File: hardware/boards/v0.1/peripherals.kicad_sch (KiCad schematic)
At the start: 8 parts, among them IC2 DA7280-00FVC, J6 VLV101040A, U21 LSM6DS3

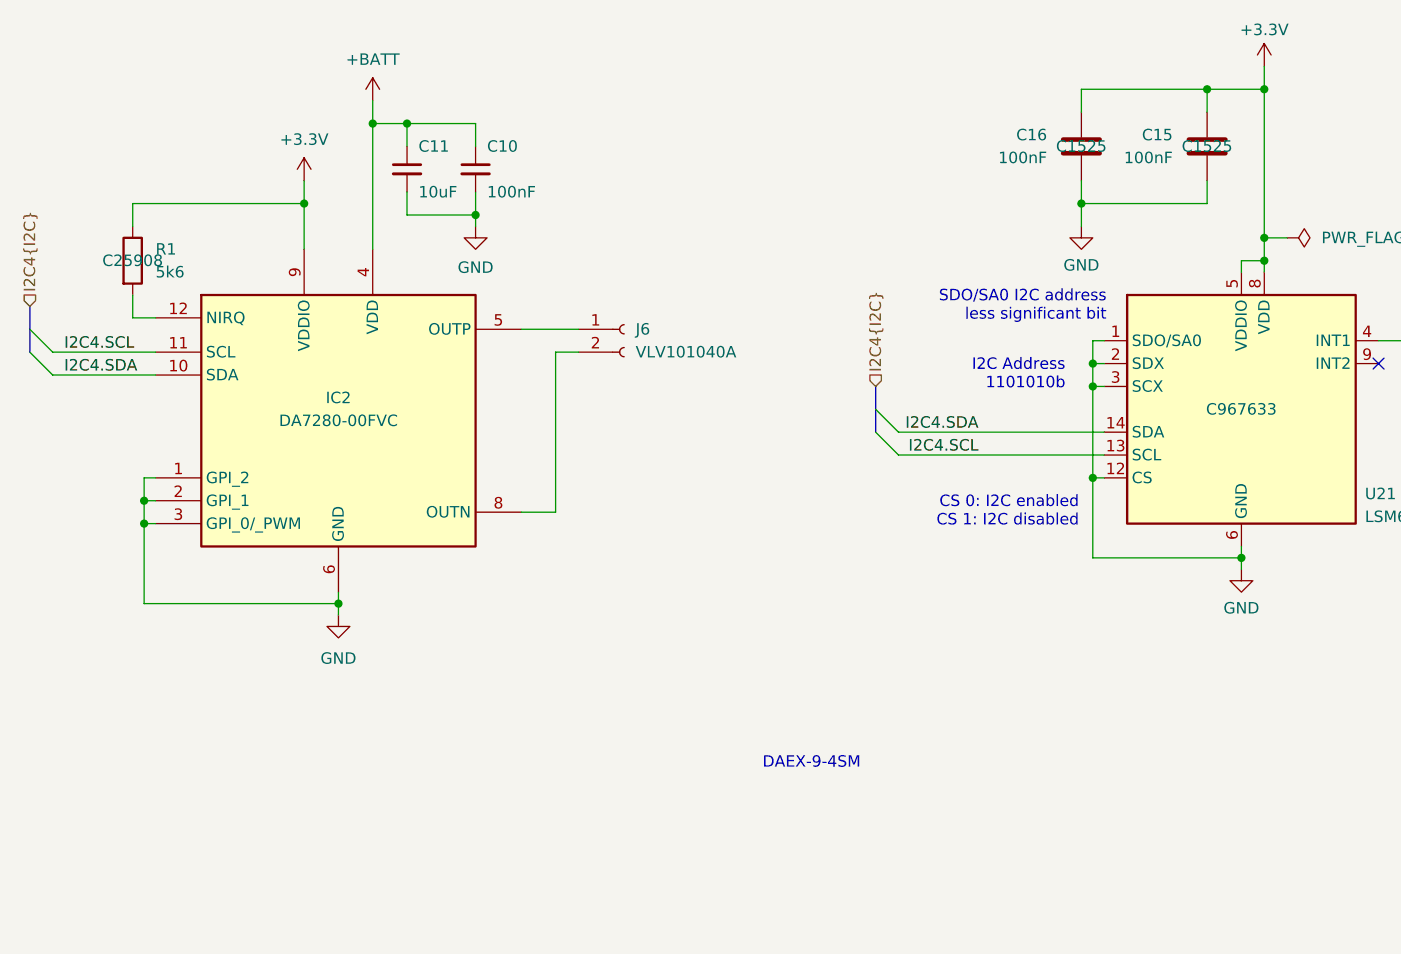
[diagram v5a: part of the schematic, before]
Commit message: feat: swap out of stock components
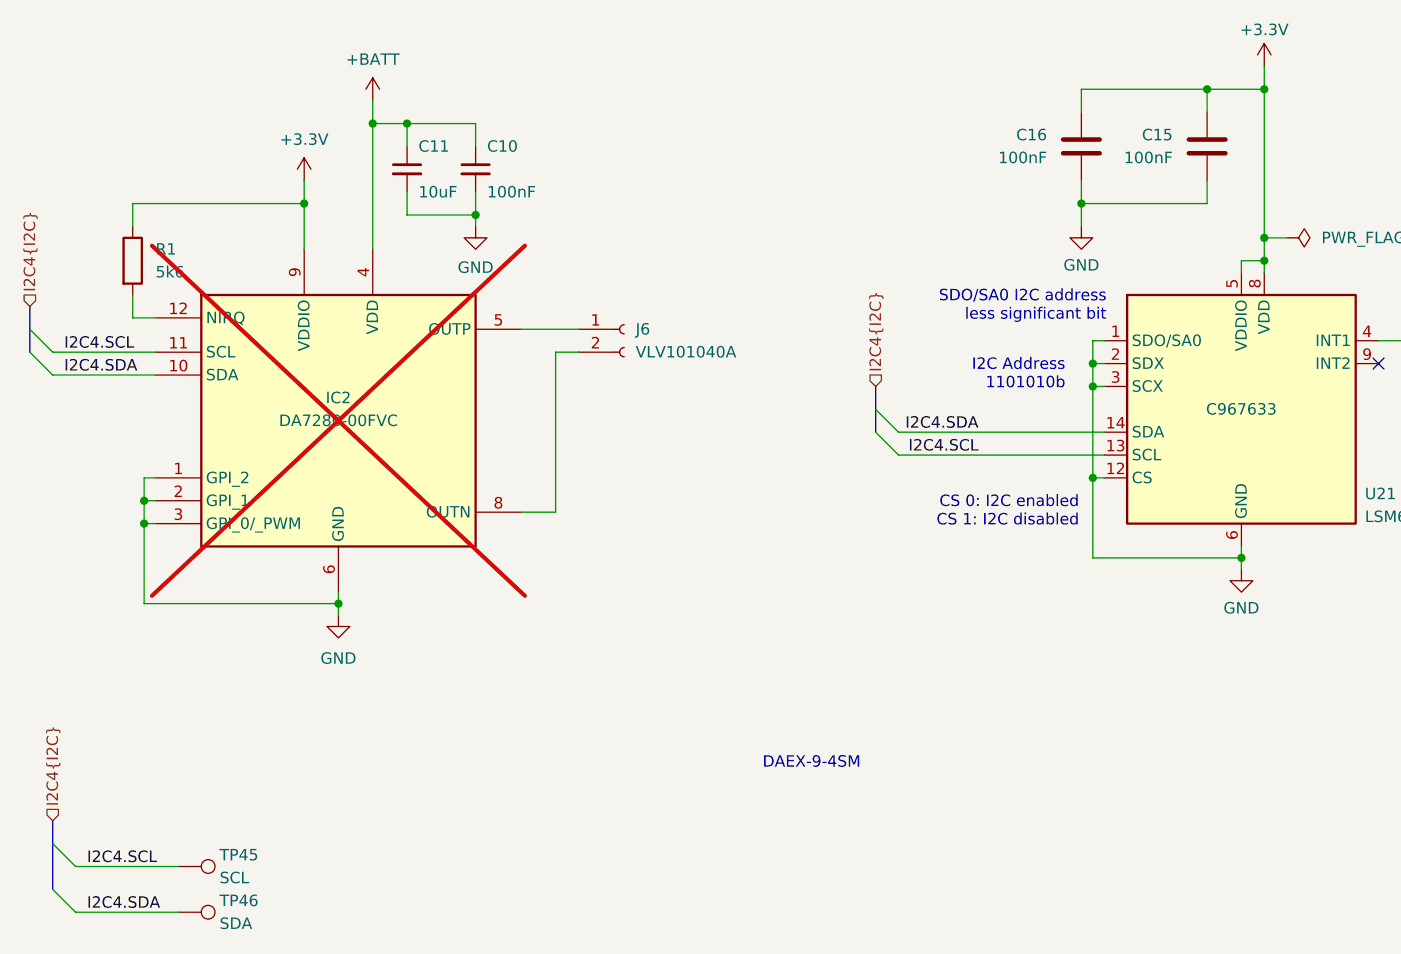
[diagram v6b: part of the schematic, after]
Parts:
- added TP45: SCL, TestPoint:TestPoint_Pad_D1.0mm, symbol Connector:TestPoint
- added TP46: SDA, TestPoint:TestPoint_Pad_D1.0mm, symbol Connector:TestPoint
- IC2: Manufacturer_Name Renesas Electronics -> (none); Manufacturer_Part_Number DA7280-00FVC -> (none); now not fitted
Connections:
- net I2C4.SCL: now also TP45.1
- net I2C4.SDA: now also TP46.1
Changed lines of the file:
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@@
+	)
+	(bus_entry
+		(at 33.02 110.49)
+		(size -2.54 -2.54)
+		(stroke
+			(width 0)
+			(type default)
+		)
 	)
 	(bus_entry
@@
 	)
 	(bus_entry
+		(at 33.02 115.57)
+		(size -2.54 -2.54)
+		(stroke
+			(width 0)
+			(type default)
+		)
+	)
+	(bus_entry
 		(at 30.48 53.34)
 		(size -2.54 -2.54)
@@
 		)
 	)
+	(wire
+		(pts
+			(xy 33.02 115.57) (xy 44.45 115.57)
+		)
+		(stroke
+			(width 0)
+			(type default)
+		)
+	)
 	(bus
 		(pts
@@
 	(wire
 		(pts
+			(xy 33.02 110.49) (xy 44.45 110.49)
+		)
+		(stroke
+			(width 0)
+			(type default)
+		)
+	)
+	(wire
+		(pts
 			(xy 39.37 46.99) (xy 39.37 49.53)
 		)
@@
 		)
 	)
+	(bus
+		(pts
+			(xy 30.48 107.95) (xy 30.48 113.03)
+		)
+		(stroke
+			(width 0)
+			(type default)
+		)
+	)
+	(bus
+		(pts
+			(xy 30.48 105.41) (xy 30.48 107.95)
+		)
+		(stroke
+			(width 0)
+			(type default)
+		)
+	)
 	(wire
 		(pts
@@
 			(width 0)
 			(type default)
+		)
+	)
+	(label "I2C4.SDA"
+		(at 34.29 115.57 0)
+		(effects
+			(font
+				(size 1.27 1.27)
+			)
+			(justify left bottom)
 		)
 	)
@@
 		)
 	)
+	(label "I2C4.SCL"
+		(at 34.29 110.49 0)
+		(effects
+			(font
+				(size 1.27 1.27)
+			)
+			(justify left bottom)
+		)
+	)
 	(label "I2C4.SDA"
 		(at 31.75 55.88 0)
@@
 		(shape input)
 		(at 121.92 57.15 90)
+		(effects
+			(font
+				(size 1.27 1.27)
+			)
+			(justify left)
+		)
+	)
+	(hierarchical_label "I2C4{I2C}"
+		(shape input)
+		(at 30.48 105.41 90)
 		(effects
 			(font
@@
 					(size 1.27 1.27)
 				)
+				(hide yes)
 			)
 		)
@@
 					(size 1.27 1.27)
 				)
+				(hide yes)
 			)
 		)
@@
 		(in_bom yes)
 		(on_board yes)
-		(dnp no)
+		(dnp yes)
 		(property "Reference" "IC2"
 			(at 62.23 58.42 0)
@@
 		(property "Height" "0.84"
 			(at 99.06 446.99 0)
-			(effects
-				(font
-					(size 1.27 1.27)
-				)
-				(justify left top)
-				(hide yes)
-			)
-		)
-		(property "Manufacturer_Name" "Renesas Electronics"
-			(at 99.06 746.99 0)
-			(effects
-				(font
-					(size 1.27 1.27)
-				)
-				(justify left top)
-				(hide yes)
-			)
-		)
-		(property "Manufacturer_Part_Number" "DA7280-00FVC"
-			(at 99.06 846.99 0)
 			(effects
 				(font
@@
 	)
 	(symbol
+		(lib_id "Connector:TestPoint")
+		(at 44.45 115.57 270)
+		(unit 1)
+		(exclude_from_sim no)
+		(in_bom no)
+		(on_board yes)
+		(dnp no)
+		(property "Reference" "TP46"
+			(at 49.022 114.3 90)
+			(effects
+				(font
+					(size 1.27 1.27)
+				)
+				(justify left)
+			)
+		)
+		(property "Value" "SDA"
+			(at 49.022 116.84 90)
+			(effects
+				(font
+					(size 1.27 1.27)
+				)
+				(justify left)
+			)
+		)
+		(property "Footprint" "TestPoint:TestPoint_Pad_D1.0mm"
+			(at 44.45 120.65 0)
+			(effects
+				(font
+					(size 1.27 1.27)
+				)
+				(hide yes)
+			)
+		)
+		(property "Datasheet" "~"
+			(at 44.45 120.65 0)
+			(effects
+				(font
+					(size 1.27 1.27)
+				)
+				(hide yes)
+			)
+		)
+		(property "Description" "test point"
+			(at 44.45 115.57 0)
+			(effects
+				(font
+					(size 1.27 1.27)
+				)
+				(hide yes)
+			)
+		)
+		(property "Part" ""
+			(at 44.45 115.57 0)
+			(effects
+				(font
+					(size 1.27 1.27)
+				)
+			)
+		)
+		(pin "1"
+		)
+		(instances
+			(project "pocket_synth"
+				(path "/485383b8-00f4-4405-b270-de249939cff4/f91e71c7-727a-4ef4-a387-8ca9d7b49c20"
+					(reference "TP46")
+					(unit 1)
+				)
+			)
+		)
+	)
+	(symbol
 		(lib_id "power:+3.3V")
 		(at 165.1 21.59 0)
@@
 				(path "/485383b8-00f4-4405-b270-de249939cff4/f91e71c7-727a-4ef4-a387-8ca9d7b49c20"
 					(reference "#PWR0102")
+					(unit 1)
+				)
+			)
+		)
+	)
+	(symbol
+		(lib_id "Connector:TestPoint")
+		(at 44.45 110.49 270)
+		(unit 1)
+		(exclude_from_sim no)
+		(in_bom no)
+		(on_board yes)
+		(dnp no)
+		(property "Reference" "TP45"
+			(at 49.022 109.22 90)
+			(effects
+				(font
+					(size 1.27 1.27)
+				)
+				(justify left)
+			)
+		)
+		(property "Value" "SCL"
+			(at 49.022 111.76 90)
+			(effects
+				(font
+					(size 1.27 1.27)
+				)
+				(justify left)
+			)
+		)
+		(property "Footprint" "TestPoint:TestPoint_Pad_D1.0mm"
+			(at 44.45 115.57 0)
+			(effects
+				(font
+					(size 1.27 1.27)
+				)
+				(hide yes)
+			)
+		)
+		(property "Datasheet" "~"
+			(at 44.45 115.57 0)
+			(effects
+				(font
+					(size 1.27 1.27)
+				)
+				(hide yes)
+			)
+		)
+		(property "Description" "test point"
+			(at 44.45 110.49 0)
+			(effects
+				(font
+					(size 1.27 1.27)
+				)
+				(hide yes)
+			)
+		)
+		(property "Part" ""
+			(at 44.45 110.49 0)
+			(effects
+				(font
+					(size 1.27 1.27)
+				)
+			)
+		)
+		(pin "1"
+		)
+		(instances
+			(project "pocket_synth"
+				(path "/485383b8-00f4-4405-b270-de249939cff4/f91e71c7-727a-4ef4-a387-8ca9d7b49c20"
+					(reference "TP45")
 					(unit 1)
 				)
@@
 					(size 1.27 1.27)
 				)
-			)
-		)
+				(hide yes)
+			)
+		)

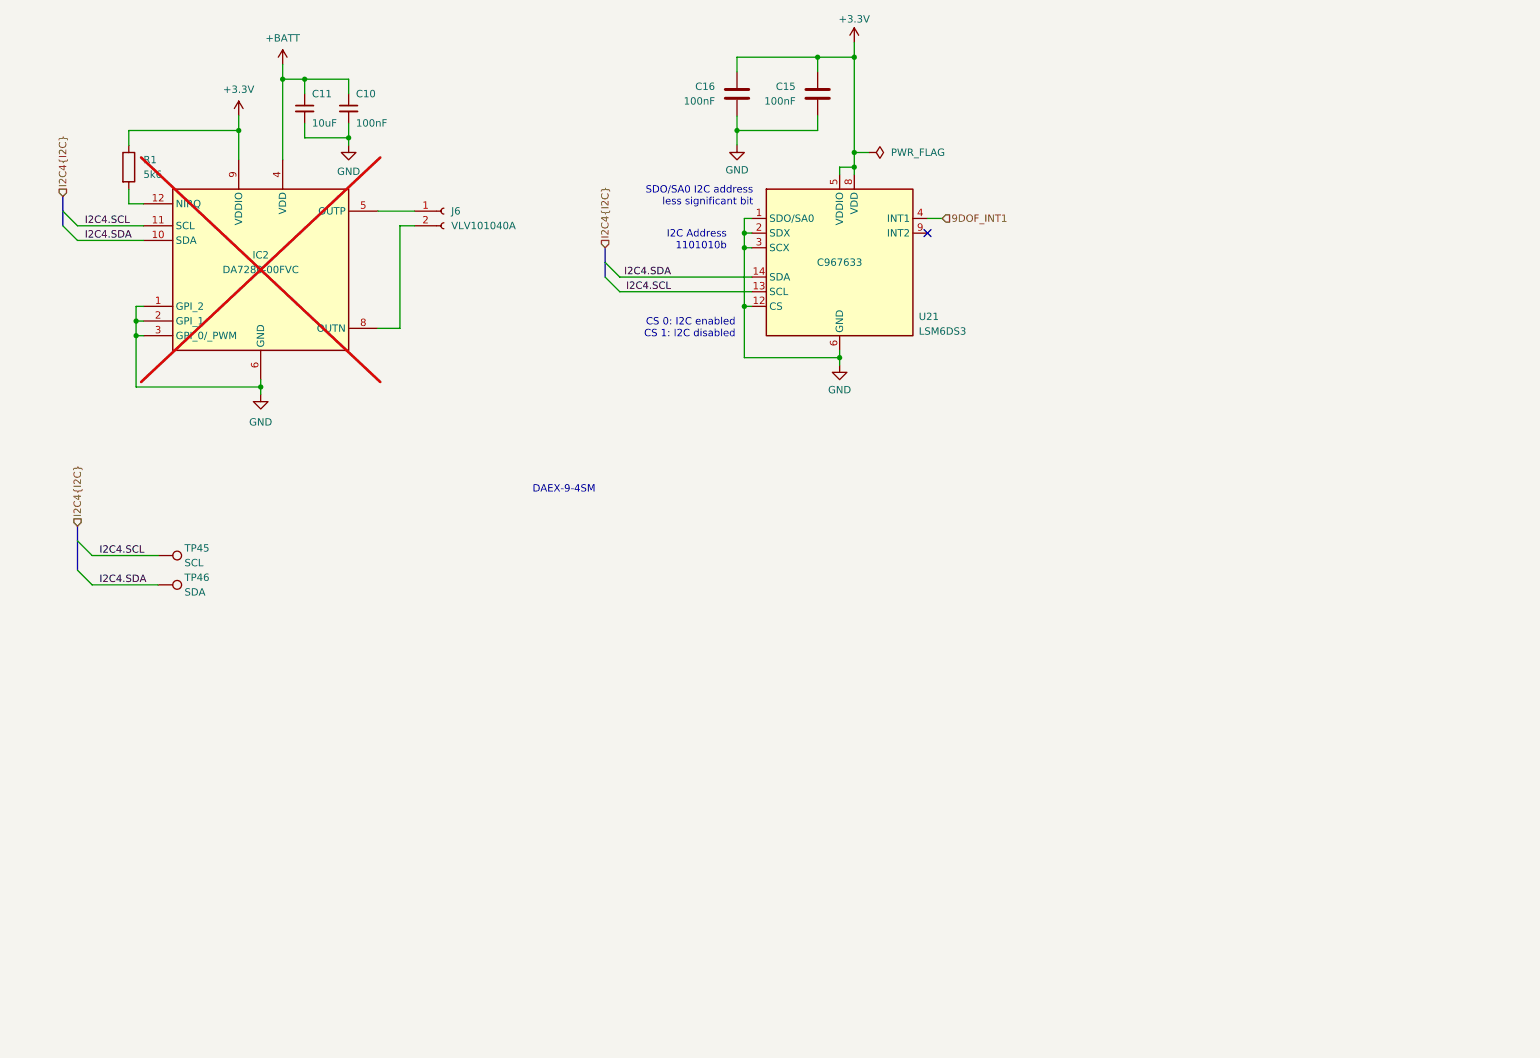
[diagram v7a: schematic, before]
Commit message: feat: add haptic transducer DAC
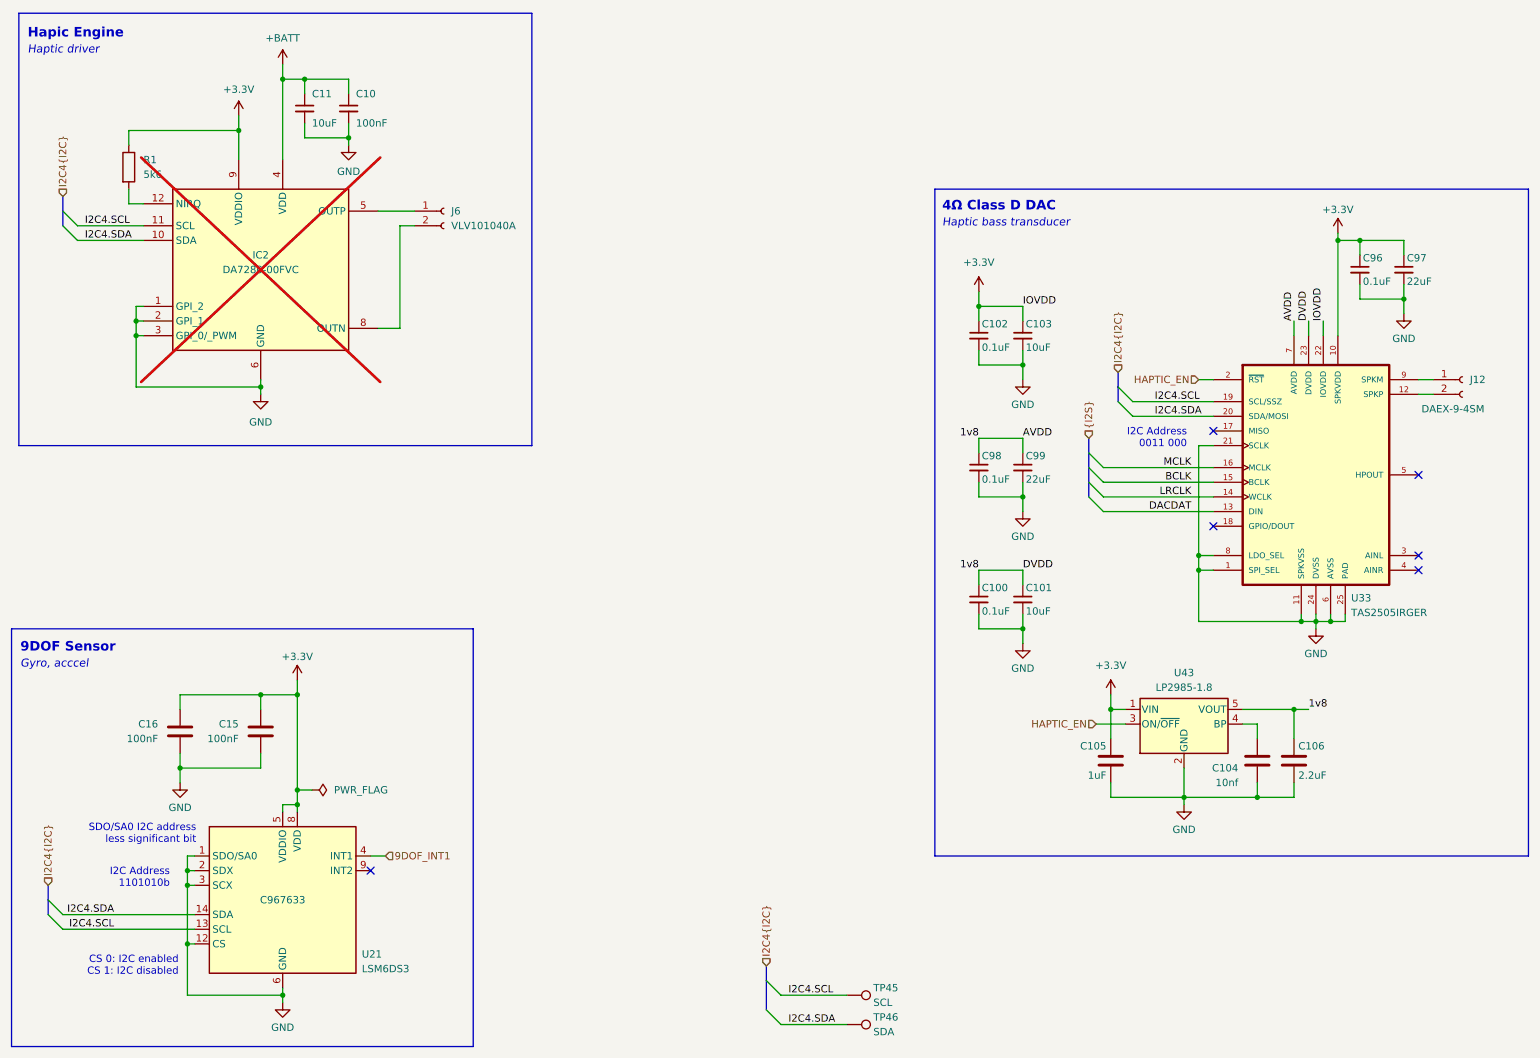
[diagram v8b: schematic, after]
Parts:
- added C100, C102, C96, C98: 0.1uF, Capacitor_SMD:C_0402_1005Metric, symbol Device:C_Small
- added C101, C103: 10uF, Capacitor_SMD:C_0402_1005Metric, symbol Device:C_Small
- added C104: 10nf, Capacitor_SMD:C_0402_1005Metric, symbol Device:C
- added C105: 1uF, Capacitor_SMD:C_0402_1005Metric, symbol Device:C
- added C106: 2.2uF, Capacitor_SMD:C_0402_1005Metric, symbol Device:C
- added C97, C99: 22uF, Capacitor_SMD:C_0402_1005Metric, symbol Device:C_Small
- added J12: DAEX-9-4SM, Connector_PinHeader_2.00mm:PinHeader_1x02_P2.00mm_Vertical, symbol Connector:Conn_01x02_Socket
- added U33: TAS2505IRGER, pocket_synth:QFN50P400X400X100-25N, symbol pocket_synth:TAS2505IRGER
- added U43: LP2985-1.8, Package_TO_SOT_SMD:SOT-23-5, symbol Regulator_Linear:LP2985-1.8
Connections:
- net +3.3V: now also C102.1, C103.1, C105.1, C96.1, C97.1, U33.10 (SPKVDD), U33.22 (IOVDD), U43.1 (VIN)
- net GND: now also C100.2, C101.2, C102.2, C103.2, C104.2, C105.2, C106.2, C96.2, C97.2, C98.2, C99.2, U33.1 (SPI_SEL), U33.11 (SPKVSS), U33.21 (SCLK), U33.24 (DVSS), U33.25 (PAD), U33.6 (AVSS), U33.8 (LDO_SEL), U43.2 (GND)
- net I2C4.SCL: now also U33.19 (SCL/SSZ)
- net I2C4.SDA: now also U33.20 (SDA/MOSI)
- new net: J12.1 (Pin_1), U33.9 (SPKM)
- new net: J12.2 (Pin_2), U33.12 (SPKP)
- new net: C104.1, U43.4 (BP)
- new net 1v8: C100.1, C101.1, C106.1, C98.1, C99.1, U33.23 (DVDD), U33.7 (AVDD), U43.5 (VOUT)
- new net BCLK: U33.15 (BCLK)
- new net DACDAT: U33.13 (DIN)
- new net HAPTIC_EN: U33.2 (~{RST}), U43.3 (ON/~{OFF})
- new net LRCLK: U33.14 (WCLK)
- new net MCLK: U33.16 (MCLK)
- no-connect marks 1 -> 6
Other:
- note added: "4Ω Class D DAC"
- note added: "9DOF Sensor"
- note added: "Gyro, acccel"
- note added: "Hapic Engine"
- note added: "Haptic bass transducer"
- note added: "Haptic driver"
- note added: "I2C Address 0011 000"
- note removed: "DAEX-9-4SM"
- moved on the sheet: C15, C16, TP45, TP46, U21
